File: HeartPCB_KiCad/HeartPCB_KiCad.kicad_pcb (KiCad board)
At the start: 2 copper layers, 68.4 x 61 mm, 47 parts, among them J1 1051640001, J3 IN-, J4 IN+, J5 B+, J6 B-, Q1 FS8205A, U1 TP4056-42-ESOP8, U2 DW01A, U5 MCP4922

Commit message: final version for order
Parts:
- turned Q1 to 0 degrees
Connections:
- GND pad 1: GND -> Net-(J8-Pin_1)
- Probe Me pad 1: Net-(J8-Pin_1) -> GND
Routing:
- net GND: track 33.0 -> 394.0 mm, vias 4 -> 6
- net /V_BAT: track 268.5 -> 275.5 mm, vias 4 -> 6
- net Net-(U2-OD): track 11.1 -> 6.85 mm
- net Net-(U3-D5): track 13.0 -> 16.8 mm
- net Net-(U3-D4): track 24.9 -> 21.3 mm
- net unconnected-(U1-EPAD-Pad9): track 3.00 -> 0.00 mm, vias 1 -> 0
- net Net-(J8-Pin_1): track 20.4 -> 18.2 mm
- net Net-(U3-D7): track 6.86 -> 8.97 mm, vias 1 -> 2
- net Net-(U2-OC): track 10.6 -> 12.4 mm
- net Net-(U3-3V3): track 40.2 -> 38.5 mm
- net Net-(U3-D9): track 34.8 -> 33.2 mm
- net +5V_USB: track 48.2 -> 46.5 mm
- net /CHRG: track 43.1 -> 41.8 mm
- net Net-(U3-D8): track 28.7 -> 27.5 mm
- net /LED_Din: track 32.5 -> 33.6 mm
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
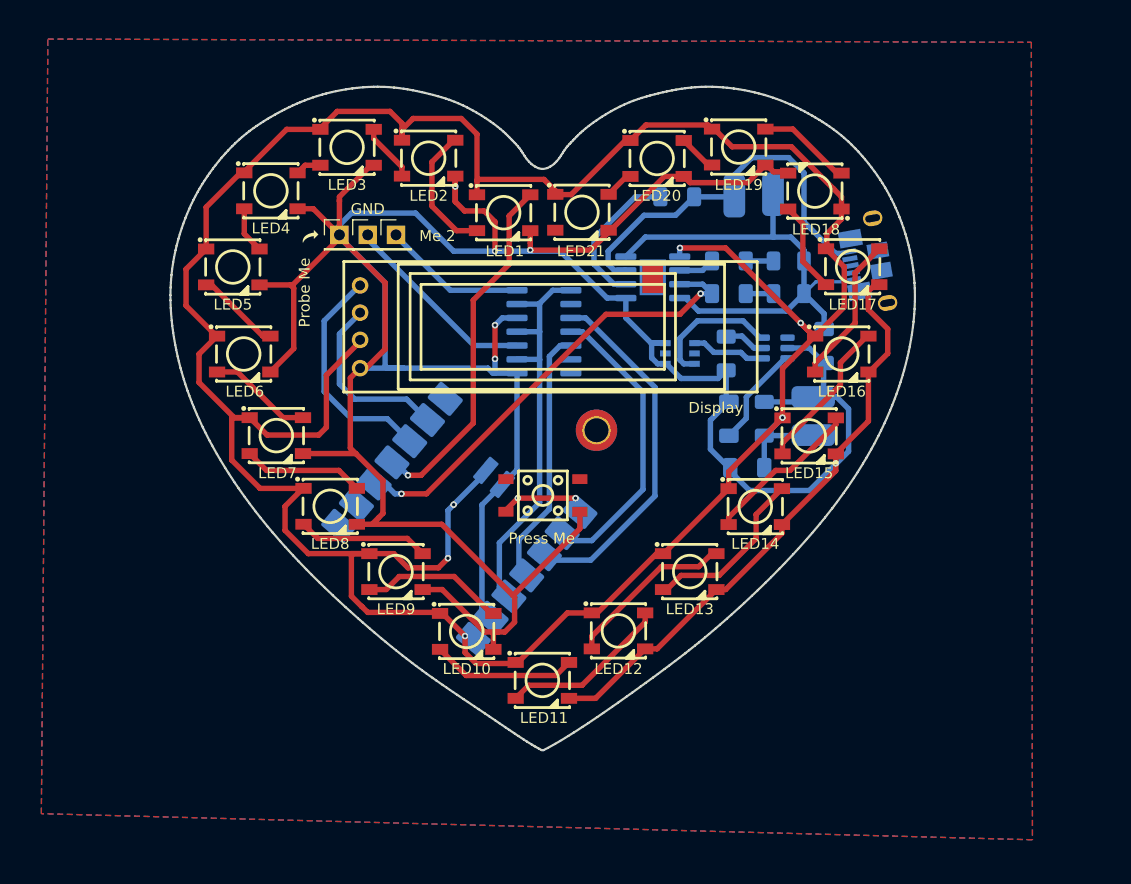
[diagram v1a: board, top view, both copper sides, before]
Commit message: fixed ra4m1 footprint
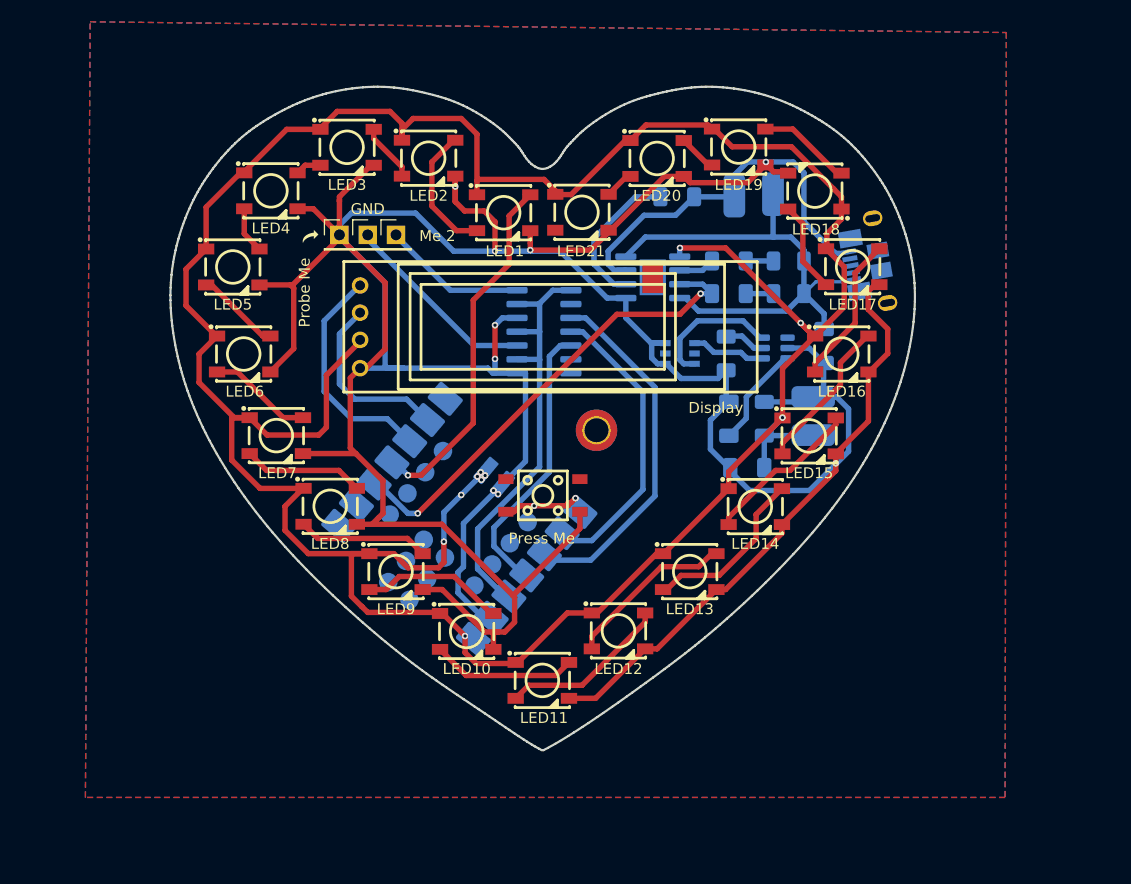
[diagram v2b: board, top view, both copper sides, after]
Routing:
- net Net-(U3-D10): track 24.0 -> 27.1 mm
- net Net-(U3-3V3): track 38.5 -> 41.6 mm
- net GND: track 394.0 -> 397.0 mm, vias 6 -> 9
- net /CHRG: track 41.8 -> 44.3 mm
- net /V_BAT: vias 6 -> 10
